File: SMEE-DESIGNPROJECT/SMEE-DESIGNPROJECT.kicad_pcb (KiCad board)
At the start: 2 copper layers, 30 x 120 mm, 15 parts, among them J1 Conn_01x05, U1 TLC555xP

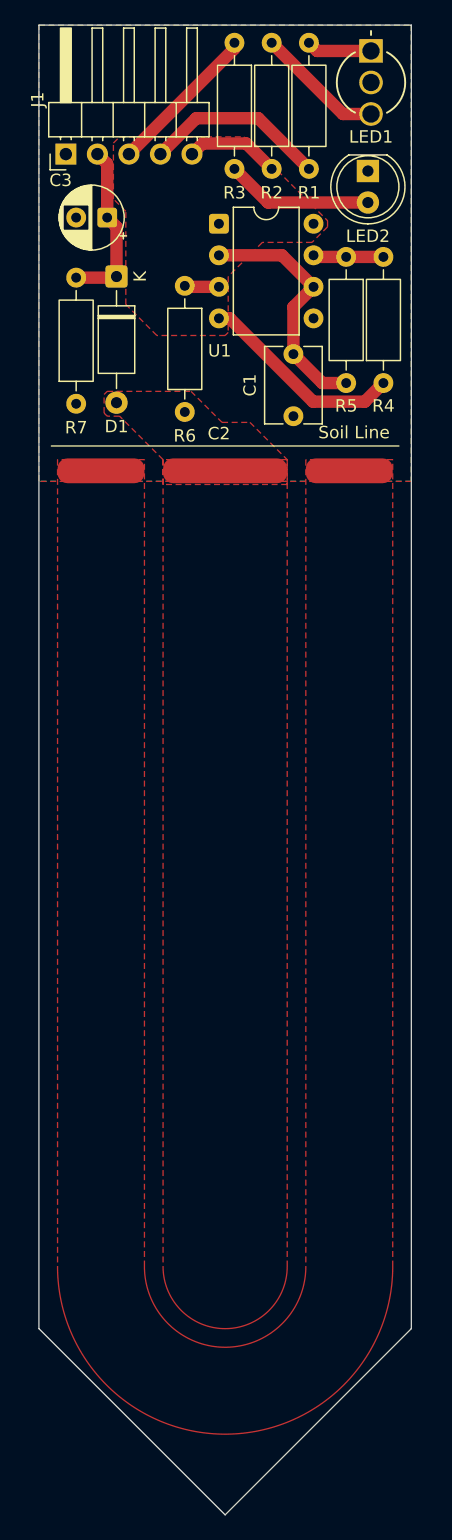
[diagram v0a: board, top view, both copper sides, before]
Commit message: Adjust footprints, stackup, and project metadata
Small KiCad project updates: tweak SMEE_SOIL_PROBE silkscreen lines and text positions (added B.SilkS line), update WP59EGW_KNB 3D model path and Z offset, and add a detailed board stackup to the .kicad_pcb. Removed teardrops from the SMEE_SOIL_PROBE footprint, updated footprint positions/visibility for some references, and regenerated many UUIDs in footprints. Project metadata files (kicad_prl, kicad_pro, fp-info-cache) were updated and several backup .zip files plus a .kicad_sch.lck file were added.
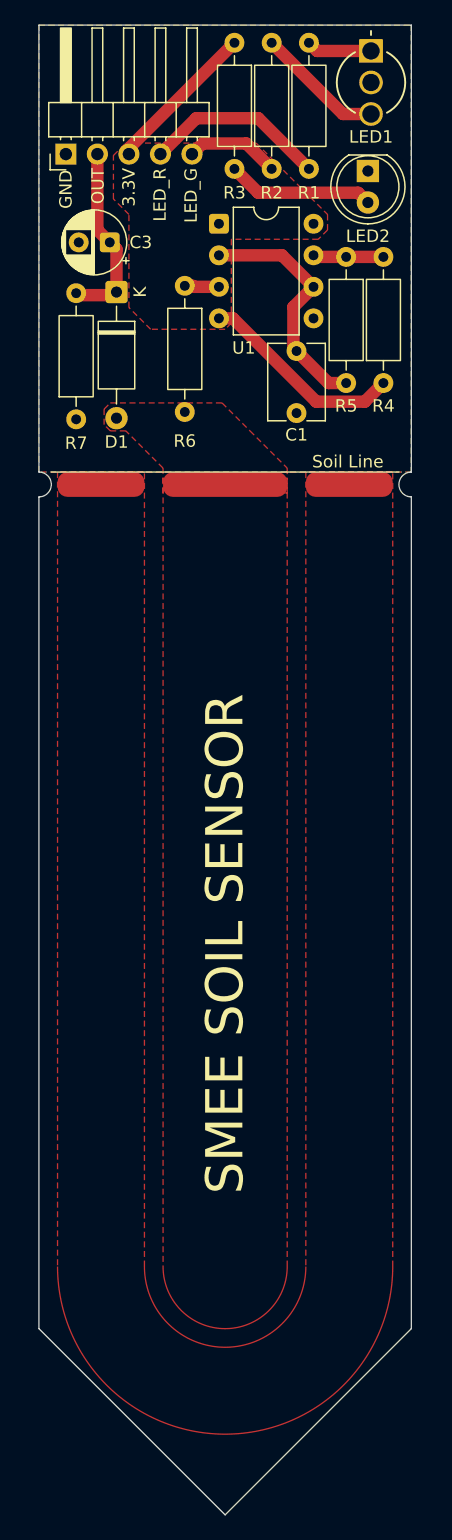
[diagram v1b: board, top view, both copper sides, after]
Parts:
- moved C3 2.01 mm to (55.7, 67.5)
- moved D1 1.25 mm to (56.2, 71.5)
- moved R7 1.25 mm to (53.0, 81.8)
- moved C2 1.10 mm to (65.0, 89.0)
- moved C1 0.35 mm to (70.8, 76.2)
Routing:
- net /RCOUT: track 13.8 -> 15.2 mm
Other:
- outline, holes or cut-outs redrawn
- board text added: "3.3V"
- board text added: "GND"
- board text added: "LED_G"
- board text added: "LED_R"
- board text added: "OUT"
- board text added: "SMEE SOIL SENSOR"

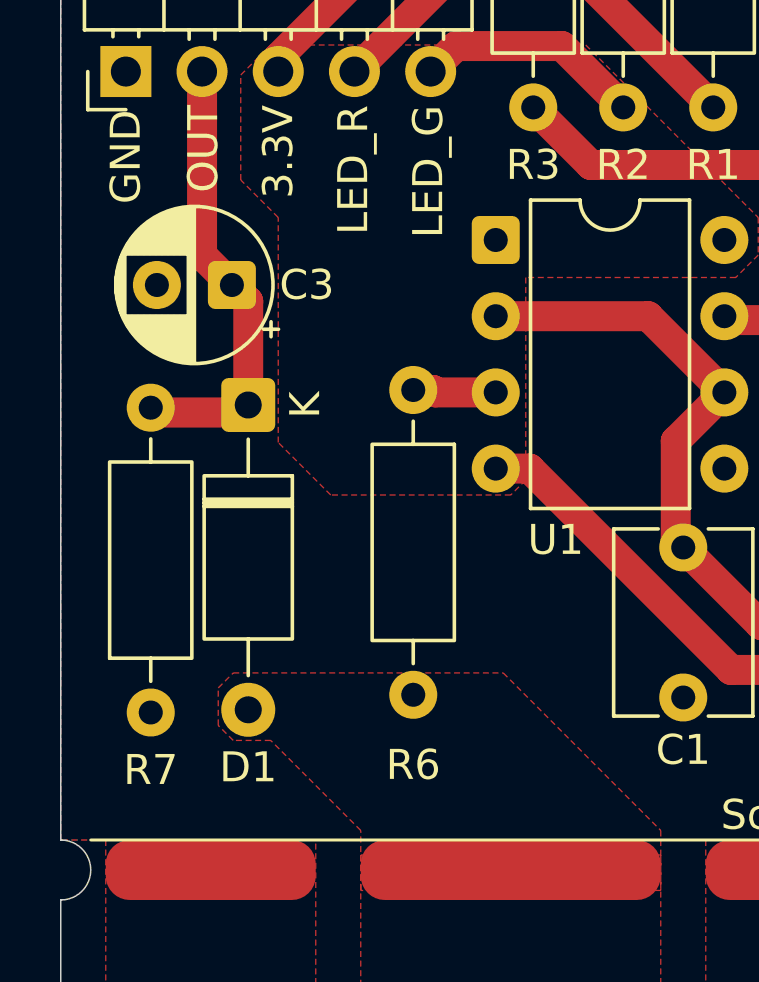
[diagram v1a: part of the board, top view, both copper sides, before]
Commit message: Adjust PCB footprints, traces and copper zones
Modify SMEE-DESIGNPROJECT.kicad_pcb to tweak component placements (small XY adjustments for axial resistor and diode), adjust trace segments (endpoints, added short segments, updated UUIDs), and reorganize copper zones/teardrop pad-via polygons and priorities. Add two backup ZIPs under SMEE-DESIGNPROJECT-backups. Also update project files (.kicad_prl, .kicad_sch). These changes address alignment and copper-pour/connection corrections on the PCB.
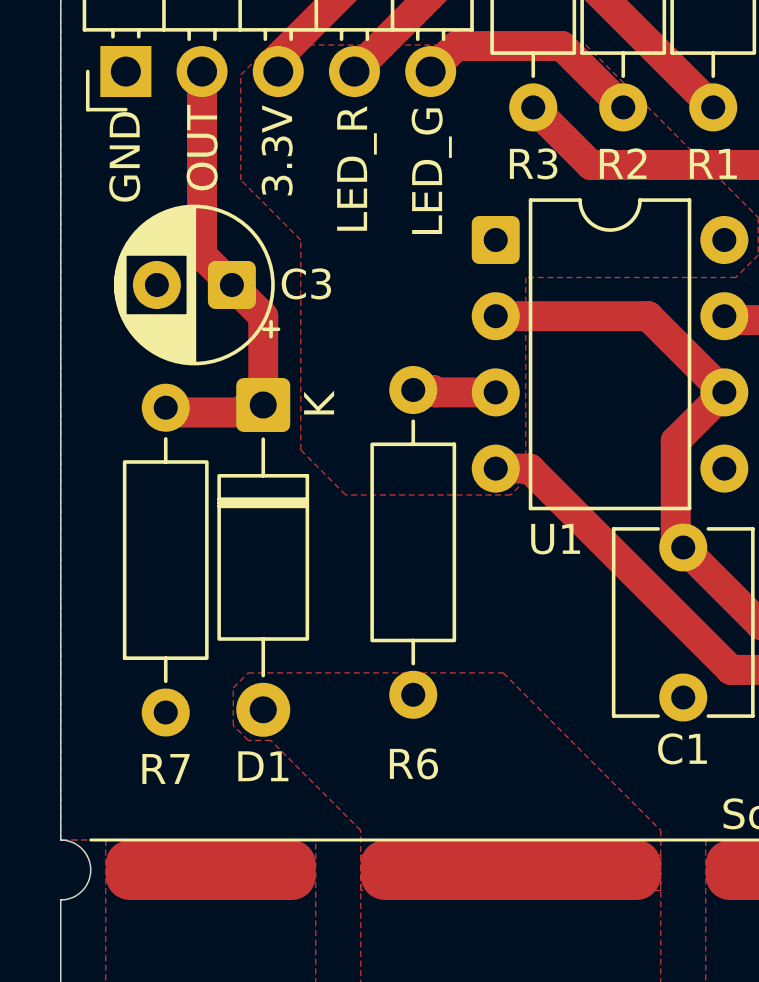
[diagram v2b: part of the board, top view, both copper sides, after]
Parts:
- moved D1 0.50 mm to (56.8, 71.5)
- moved R7 0.50 mm to (53.5, 81.8)

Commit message: Add fabrication outputs; tweak footprint
Adjust SMD pad geometry in SMEE_SOIL_PROBE.kicad_mod (minor position/size changes). Add generated fabrication outputs (Gerbers, drill files, edge cuts) and a ZIP export. Update project files (.kicad_pcb, .kicad_prl, .kicad_pro) and fp-info-cache, add two new backup zips and remove an older backup.
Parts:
- C1: value 1n -> 10p
- R5: value 1k -> 220k

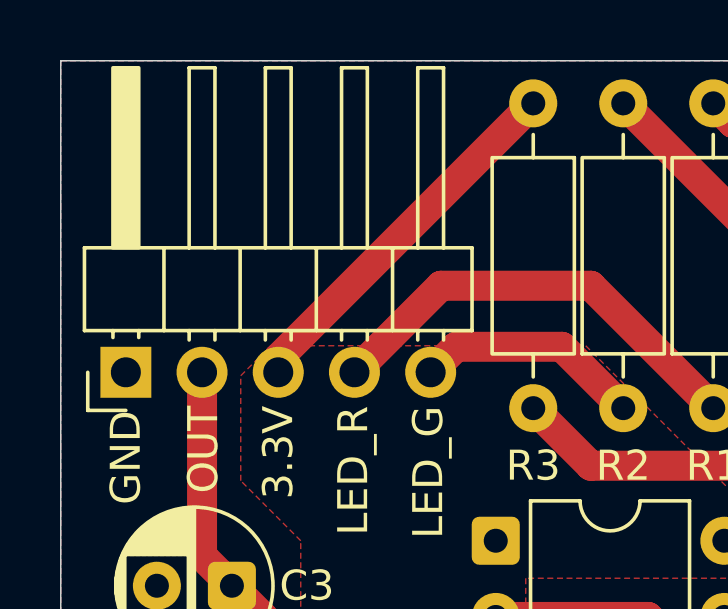
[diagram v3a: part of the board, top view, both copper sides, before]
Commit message: Enable teardrops on pads and add teardrop zones
Enable teardrops for numerous pads in SMEE-DESIGNPROJECT.kicad_pcb (added teardrops blocks with parameters like best_length_ratio, max_length, best_width_ratio, max_width, filter_ratio, enabled, allow_two_segments, prefer_zone_connections). Add two $teardrop_padvia$ zones to support pad/via teardrops and updated polygon/fill data. Also adjust a J1 footprint reference position, replace an old backup ZIP with a new one, remove KiCad lock files, and update the .kicad_prl/.kicad_pcb accordingly.
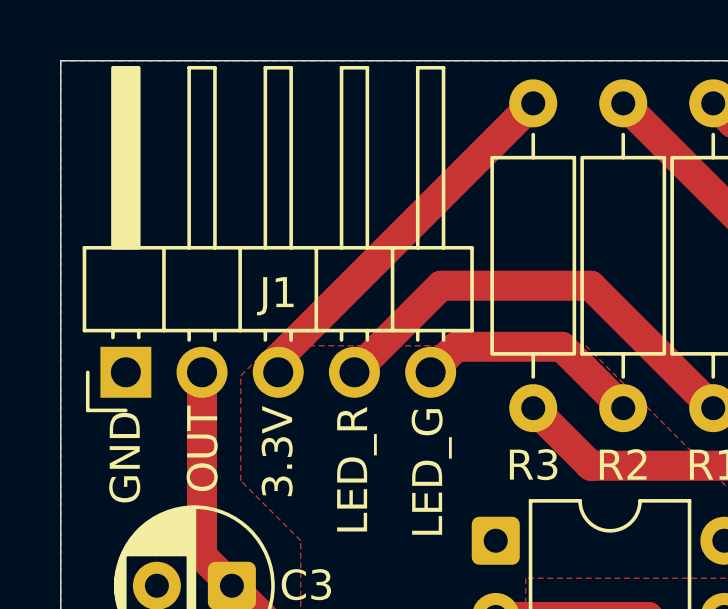
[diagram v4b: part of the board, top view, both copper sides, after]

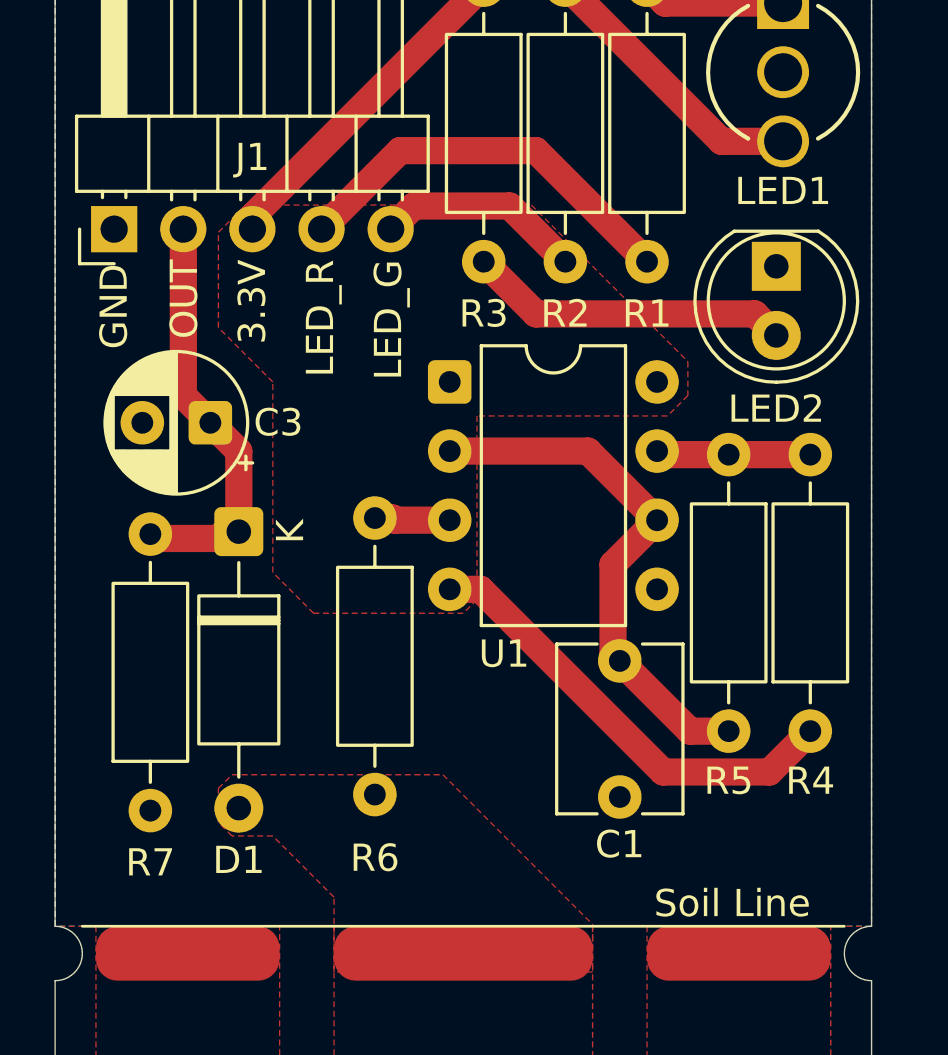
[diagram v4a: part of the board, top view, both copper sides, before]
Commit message: SMEE PCB: renumber nets, adjust zones & footprints
Remove/replace old backup zips and add lock files; update SMEE-DESIGNPROJECT.kicad_pcb with net renumbering and reassignments, footprint position/UUID tweaks, trace segment coordinate changes, and zone updates (including a new teardrop padvia zone and adjusted zone net names/priorities). These edits reflect routing corrections, component placement tweaks, and teardrop/padvia additions for manufacturing reliability.
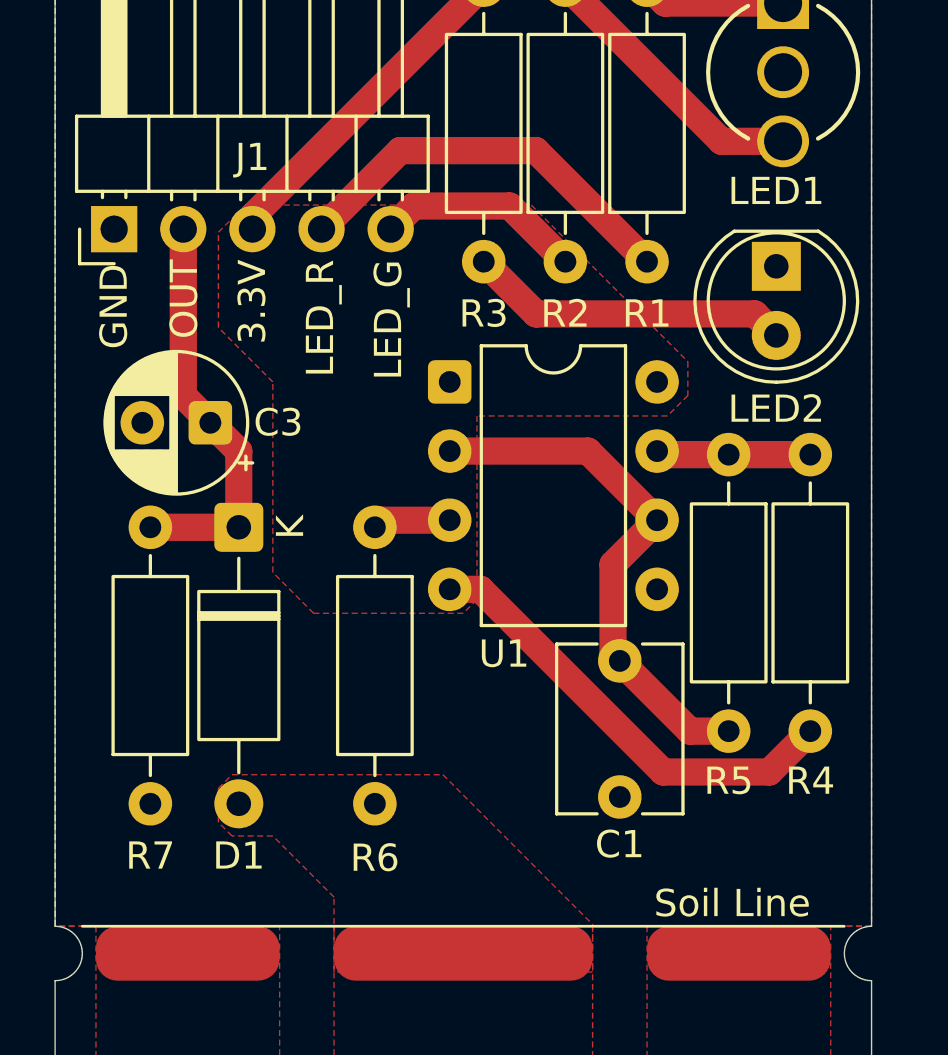
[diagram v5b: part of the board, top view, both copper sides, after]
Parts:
- moved R6 0.34 mm to (61.8, 71.3)
- moved R7 0.25 mm to (53.5, 81.5)
- moved D1 0.16 mm to (56.8, 71.3)

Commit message: Update PCB footprints, positions and UUIDs
Add a project backup ZIP and apply multiple KiCad PCB updates: replace many element UUIDs, adjust component positions/rotations (notably LED2 and a radial capacitor footprint changed to 2.00mm pitch), flip pad orientations to 90°, and update numerous silk/FP geometry coordinates and arcs to match adjusted footprints. These changes align footprints and silks with the revised component geometry and include minor metadata updates.
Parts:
- C3: footprint Capacitor_THT:CP_Radial_D5.0mm_P2.50mm -> Capacitor_THT:CP_Radial_D5.0mm_P2.00mm
- D1: footprint Diode_THT:D_A-405_P10.16mm_Horizontal -> Diode_THT:D_DO-35_SOD27_P10.16mm_Horizontal
- moved R3 10.2 mm to (65.8, 61.6), turned to 90 degrees
- moved LED2 2.75 mm to (76.5, 64.5), turned to 90 degrees
- moved D1 0.50 mm to (56.2, 71.3)
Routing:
- net +3.3V: track 29.1 -> 16.7 mm
- net Net-(U1-DIS): track 5.68 -> 0.00 mm
- net Net-(LED2-A): track 11.9 -> 15.1 mm
- net /RCOUT: track 15.0 -> 14.3 mm
